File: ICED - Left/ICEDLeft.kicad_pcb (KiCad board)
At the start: 2 copper layers, 175.4 x 145 mm, 164 parts, among them P1 FLASH_HDR, P2 USBC, P3 CONN_17, P4 USB3_AFEMALE, Q1 TC1264, U1 MK20DX256VLH7, U2 IS31FL3731C, X1 CRYSTAL

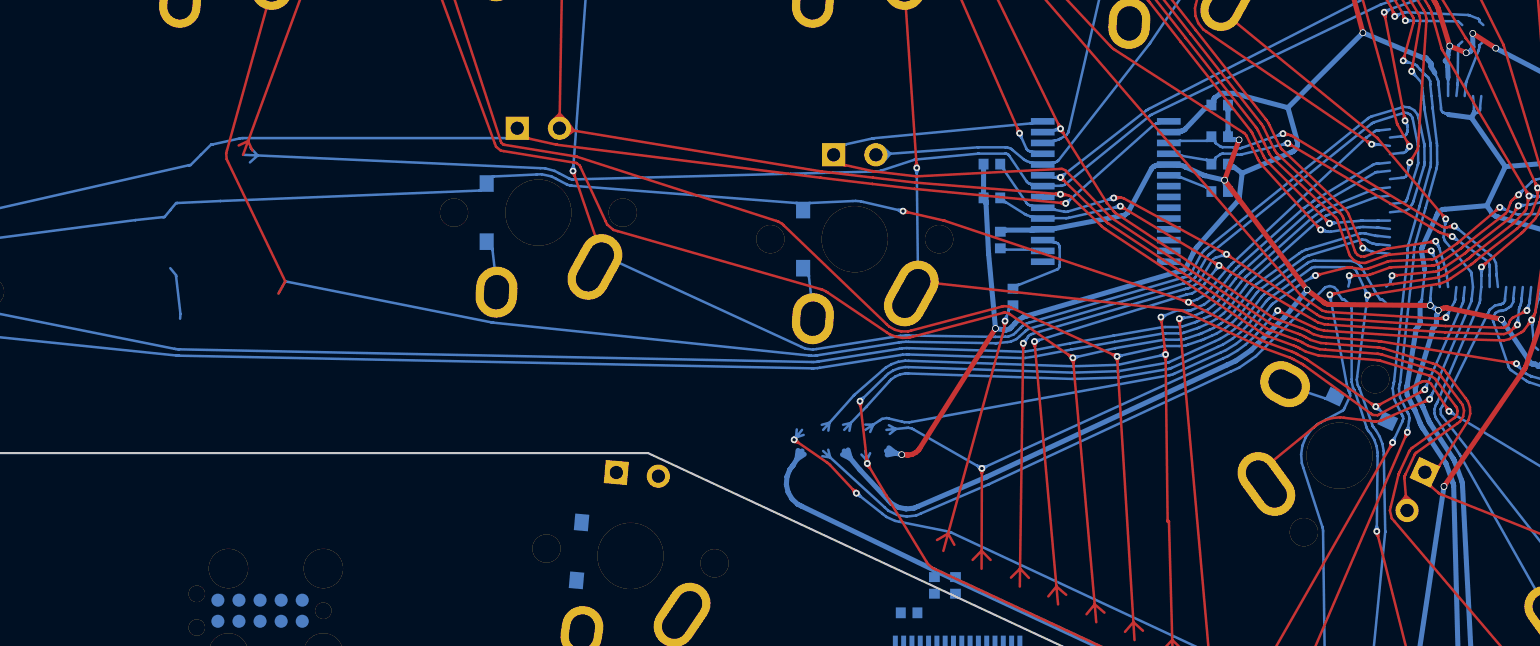
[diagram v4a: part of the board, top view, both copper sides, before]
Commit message: moved U2 and S33-S35
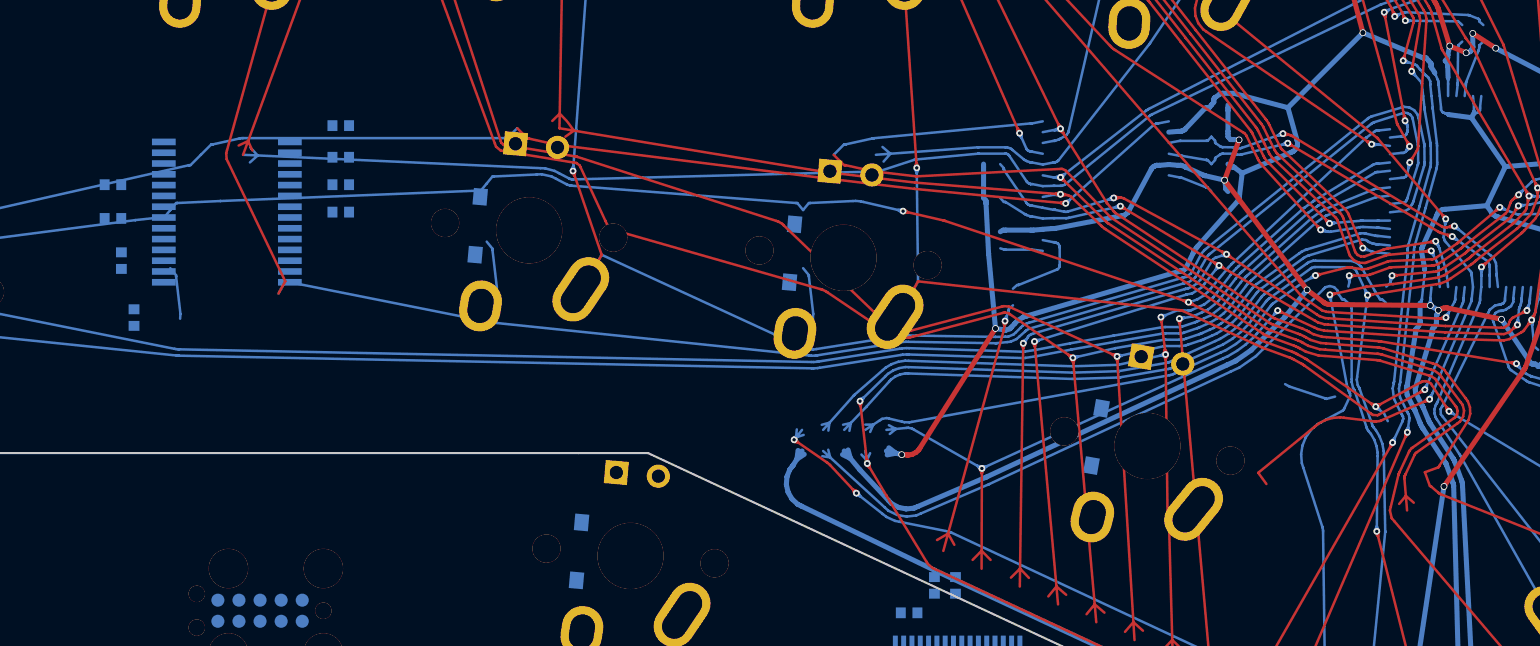
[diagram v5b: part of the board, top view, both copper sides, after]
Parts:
- moved U2 52.9 mm to (69.0, 121.0)
- moved C8 52.9 mm to (63.4, 127.3)
- moved C9 52.9 mm to (62.6, 123.9)
- moved R4 52.9 mm to (62.1, 119.3)
- moved R5 52.9 mm to (62.1, 121.4)
- moved C6 52.9 mm to (75.9, 115.8)
- moved R12 52.9 mm to (75.9, 121.0)
- moved R3 52.9 mm to (75.9, 119.3)
- moved R8 52.9 mm to (75.9, 117.7)
- moved D71 17.2 mm to (125.3, 129.9), turned to 350 degrees
- moved D33 16.0 mm to (121.4, 134.5), turned to 170 degrees
- moved S33 11.6 mm to (124.4, 135.1), turned to 170 degrees
- moved S34 1.31 mm to (106.1, 123.8), turned to 175 degrees
- moved S35 1.20 mm to (87.2, 122.1), turned to 175 degrees
- moved D72 1.13 mm to (106.6, 118.7), turned to 355 degrees
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
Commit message: Checkpoint, moving S32.
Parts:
- moved D70 37.5 mm to (142.5, 111.6), turned to 280 degrees
- moved D32 24.3 mm to (147.0, 117.9), turned to 100 degrees
- moved S32 23.5 mm to (147.5, 120.9), turned to 100 degrees
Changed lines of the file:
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@@
   )
   (module prettylib:INSW_LEDS_REG (layer Front)
-    (at 157.861 145.864 245)
-    (attr smd)
-    (fp_text reference D70 (at 0 -1.5 245) (layer B.SilkS)
-      (effects (font (size 1 1) (thickness 0.2)) (justify mirror))
-    )
-    (fp_text value LED (at 0 2.413 245) (layer F.SilkS) hide
-      (effects (font (thickness 0.3048)))
-    )
-    (pad 2 thru_hole oval (at 1.27 0 245) (size 1.4 1.4) (drill 0.8) (layers *.Cu *.Mask F.SilkS)
+    (at 142.50469 111.64536 280)
+    (attr smd)
+    (fp_text reference D70 (at 0 -1.5 280) (layer B.SilkS)
+      (effects (font (size 1 1) (thickness 0.2)) (justify mirror))
+    )
+    (fp_text value LED (at 0 2.413 280) (layer F.SilkS) hide
+      (effects (font (thickness 0.3048)))
+    )
+    (pad 2 thru_hole oval (at 1.27 0 280) (size 1.4 1.4) (drill 0.8) (layers *.Cu *.Mask F.SilkS)
       (net 3 /ledmatrix/CA2))
-    (pad 1 thru_hole rect (at -1.27 0 245) (size 1.4 1.4) (drill 0.8) (layers *.Cu *.Mask F.SilkS)
+    (pad 1 thru_hole rect (at -1.27 0 280) (size 1.4 1.4) (drill 0.8) (layers *.Cu *.Mask F.SilkS)
       (net 9 /ledmatrix/CA8))
   )
@@
   )
   (module prettylib:SOT123-DIODE (layer Back)
-    (at 154.574 140.899 65)
-    (descr DIODE)
-    (tags DIODE)
-    (attr smd)
-    (fp_text reference D32 (at 0 3.81 335) (layer B.SilkS)
-      (effects (font (size 1.016 1.016) (thickness 0.2032)) (justify mirror))
-    )
-    (fp_text value DIODE (at 2.031999 0 335) (layer B.SilkS) hide
-      (effects (font (thickness 0.3048)) (justify mirror))
-    )
-    (fp_line (start -0.8509 0.70104) (end 0.8509 0.70104) (layer B.SilkS) (width 0.22098))
-    (fp_line (start -0.8509 1.45034) (end -0.59944 1.45034) (layer B.SilkS) (width 0.22098))
-    (fp_line (start 0.8509 1.45034) (end 0.59944 1.45034) (layer B.SilkS) (width 0.22098))
-    (fp_line (start 0.8509 -1.45034) (end 0.59944 -1.45034) (layer B.SilkS) (width 0.22098))
-    (fp_line (start -0.8509 -1.45034) (end -0.59944 -1.45034) (layer B.SilkS) (width 0.22098))
-    (fp_line (start -0.8509 -1.45034) (end -0.8509 1.45034) (layer B.SilkS) (width 0.22098))
-    (fp_line (start 0.8509 -1.45034) (end 0.8509 1.45034) (layer B.SilkS) (width 0.22098))
-    (pad 2 smd rect (at 0 1.7526 155) (size 1.00076 0.8509) (layers Back B.Paste B.Mask)
+    (at 146.96729 117.85944 100)
+    (descr DIODE)
+    (tags DIODE)
+    (attr smd)
+    (fp_text reference D32 (at 0 3.81 370) (layer B.SilkS)
+      (effects (font (size 1.016 1.016) (thickness 0.2032)) (justify mirror))
+    )
+    (fp_text value DIODE (at 2.031999 0 370) (layer B.SilkS) hide
+      (effects (font (thickness 0.3048)) (justify mirror))
+    )
+    (fp_line (start -0.8509 0.70104) (end 0.8509 0.70104) (layer B.SilkS) (width 0.22098))
+    (fp_line (start -0.8509 1.45034) (end -0.59944 1.45034) (layer B.SilkS) (width 0.22098))
+    (fp_line (start 0.8509 1.45034) (end 0.59944 1.45034) (layer B.SilkS) (width 0.22098))
+    (fp_line (start 0.8509 -1.45034) (end 0.59944 -1.45034) (layer B.SilkS) (width 0.22098))
+    (fp_line (start -0.8509 -1.45034) (end -0.59944 -1.45034) (layer B.SilkS) (width 0.22098))
+    (fp_line (start -0.8509 -1.45034) (end -0.8509 1.45034) (layer B.SilkS) (width 0.22098))
+    (fp_line (start 0.8509 -1.45034) (end 0.8509 1.45034) (layer B.SilkS) (width 0.22098))
+    (pad 2 smd rect (at 0 1.7526 190) (size 1.00076 0.8509) (layers Back B.Paste B.Mask)
       (net 101 /Row5))
-    (pad 1 smd rect (at 0 -1.74752 155) (size 1.00076 0.8509) (layers Back B.Paste B.Mask)
+    (pad 1 smd rect (at 0 -1.74752 190) (size 1.00076 0.8509) (layers Back B.Paste B.Mask)
       (net 80 "Net-(D32-Pad1)"))
   )
@@
   )
   (module prettylib:MXALPS (layer Front)
-    (at 153.258 143.718 65)
+    (at 147.50752 120.92323 100)
     (descr MXALPS)
     (tags MXALPS)
-    (fp_text reference S32 (at 0 3.048 65) (layer B.SilkS)
-      (effects (font (thickness 0.3048)) (justify mirror))
-    )
-    (fp_text value SW (at -3.5 9 65) (layer B.SilkS) hide
+    (fp_text reference S32 (at 0 3.048 100) (layer B.SilkS)
+      (effects (font (thickness 0.3048)) (justify mirror))
+    )
+    (fp_text value SW (at -3.5 9 100) (layer B.SilkS) hide
       (effects (font (thickness 0.3048)) (justify mirror))
     )
@@
     (fp_line (start 7.62 7.62) (end -7.62 7.62) (layer Dwgs.User) (width 0.3))
     (fp_line (start -7.62 7.62) (end -7.62 -7.62) (layer Dwgs.User) (width 0.3))
-    (pad "" np_thru_hole circle (at 0 0 65) (size 3.98781 3.98781) (drill 3.9878) (layers *.Cu *.Mask F.SilkS)
+    (pad "" np_thru_hole circle (at 0 0 100) (size 3.98781 3.98781) (drill 3.9878) (layers *.Cu *.Mask F.SilkS)
       (clearance 0.1524))
-    (pad "" np_thru_hole circle (at -5.08 0 65) (size 1.70181 1.70181) (drill 1.7018) (layers *.Cu *.Mask F.SilkS)
+    (pad "" np_thru_hole circle (at -5.08 0 100) (size 1.70181 1.70181) (drill 1.7018) (layers *.Cu *.Mask F.SilkS)
       (clearance 0.1524))
-    (pad "" np_thru_hole circle (at 5.08 0 65) (size 1.70181 1.70181) (drill 1.7018) (layers *.Cu *.Mask F.SilkS)
+    (pad "" np_thru_hole circle (at 5.08 0 100) (size 1.70181 1.70181) (drill 1.7018) (layers *.Cu *.Mask F.SilkS)
       (clearance 0.1524))
-    (pad 1 thru_hole oval (at -3.405 -3.27 35.95) (size 2.5 4.17) (drill oval 1.5 3.17) (layers *.Cu *.Mask F.SilkS)
+    (pad 1 thru_hole oval (at -3.405 -3.27 70.95) (size 2.5 4.17) (drill oval 1.5 3.17) (layers *.Cu *.Mask F.SilkS)
       (net 113 /Col3))
-    (pad 2 thru_hole oval (at 2.52 -4.79 61.1) (size 2.5 3.08) (drill oval 1.5 2.08) (layers *.Cu *.Mask F.SilkS)
+    (pad 2 thru_hole oval (at 2.52 -4.79 96.1) (size 2.5 3.08) (drill oval 1.5 2.08) (layers *.Cu *.Mask F.SilkS)
       (net 80 "Net-(D32-Pad1)"))
   )

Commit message: moved S32
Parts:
- moved D70 13.1 mm to (152.5, 120.0)
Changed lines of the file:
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@@
   )
   (module prettylib:INSW_LEDS_REG (layer Front)
-    (at 142.50469 111.64536 280)
+    (at 152.51034 120.0411 280)
     (attr smd)
     (fp_text reference D70 (at 0 -1.5 280) (layer B.SilkS)

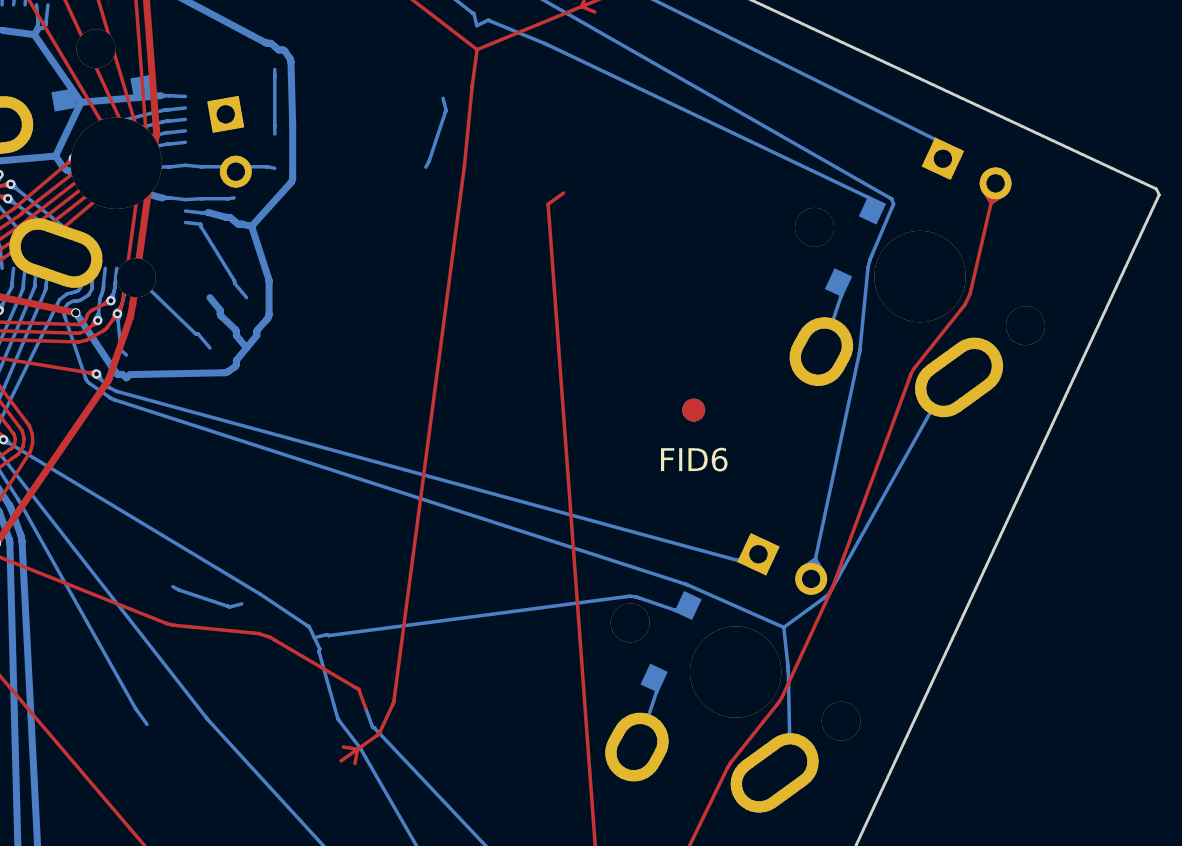
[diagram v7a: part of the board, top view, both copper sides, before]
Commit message: moved S21
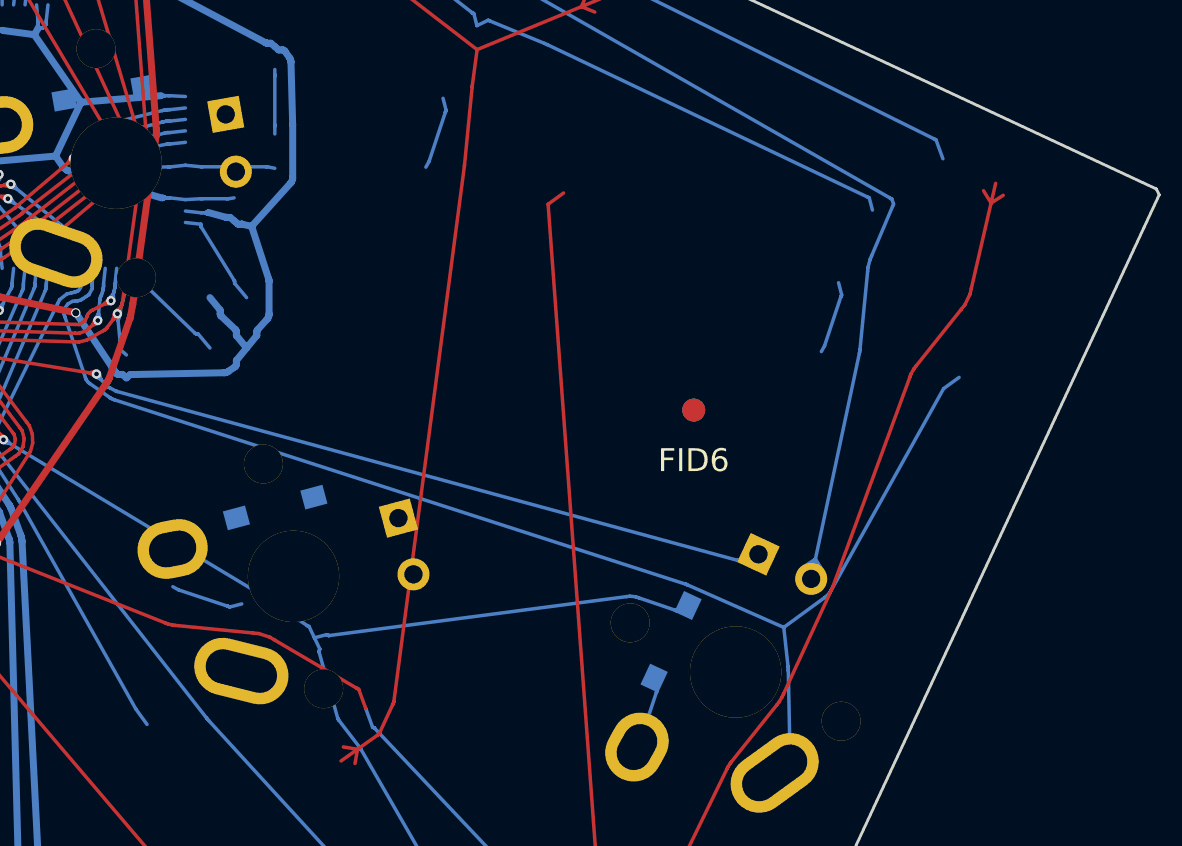
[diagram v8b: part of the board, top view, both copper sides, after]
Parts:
- moved S21 30.3 mm to (155.2, 139.0), turned to 105 degrees
- moved D59 29.5 mm to (160.2, 137.6), turned to 285 degrees
- moved D21 27.8 mm to (154.4, 136.0), turned to 105 degrees
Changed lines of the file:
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@@
   )
   (module prettylib:INSW_LEDS_REG (layer Front)
-    (at 184.747 121.265 335)
-    (attr smd)
-    (fp_text reference D59 (at 0 -1.5 335) (layer B.SilkS)
+    (at 160.15609 137.64268 285)
+    (attr smd)
+    (fp_text reference D59 (at 0 -1.5 285) (layer B.SilkS)
       (effects (font (size 1 1) (thickness 0.2)) (justify mirror))
     )
-    (fp_text value LED (at 0 2.413 335) (layer F.SilkS) hide
+    (fp_text value LED (at 0 2.413 285) (layer F.SilkS) hide
       (effects (font (thickness 0.3048)))
     )
-    (pad 2 thru_hole oval (at 1.27 0 335) (size 1.4 1.4) (drill 0.8) (layers *.Cu *.Mask F.SilkS)
+    (pad 2 thru_hole oval (at 1.27 0 285) (size 1.4 1.4) (drill 0.8) (layers *.Cu *.Mask F.SilkS)
       (net 2 /ledmatrix/CA1))
-    (pad 1 thru_hole rect (at -1.27 0 335) (size 1.4 1.4) (drill 0.8) (layers *.Cu *.Mask F.SilkS)
+    (pad 1 thru_hole rect (at -1.27 0 285) (size 1.4 1.4) (drill 0.8) (layers *.Cu *.Mask F.SilkS)
       (net 7 /ledmatrix/CA6))
   )
@@
   )
   (module prettylib:SOT123-DIODE (layer Back)
-    (at 179.779 124.556 155)
-    (descr DIODE)
-    (tags DIODE)
-    (attr smd)
-    (fp_text reference D21 (at 0 3.81 425) (layer B.SilkS)
-      (effects (font (size 1.016 1.016) (thickness 0.2032)) (justify mirror))
-    )
-    (fp_text value DIODE (at 2.031999 0 425) (layer B.SilkS) hide
-      (effects (font (thickness 0.3048)) (justify mirror))
-    )
-    (fp_line (start -0.8509 0.70104) (end 0.8509 0.70104) (layer B.SilkS) (width 0.22098))
-    (fp_line (start -0.8509 1.45034) (end -0.59944 1.45034) (layer B.SilkS) (width 0.22098))
-    (fp_line (start 0.8509 1.45034) (end 0.59944 1.45034) (layer B.SilkS) (width 0.22098))
-    (fp_line (start 0.8509 -1.45034) (end 0.59944 -1.45034) (layer B.SilkS) (width 0.22098))
-    (fp_line (start -0.8509 -1.45034) (end -0.59944 -1.45034) (layer B.SilkS) (width 0.22098))
-    (fp_line (start -0.8509 -1.45034) (end -0.8509 1.45034) (layer B.SilkS) (width 0.22098))
-    (fp_line (start 0.8509 -1.45034) (end 0.8509 1.45034) (layer B.SilkS) (width 0.22098))
-    (pad 2 smd rect (at 0 1.7526 245) (size 1.00076 0.8509) (layers Back B.Paste B.Mask)
+    (at 154.44421 135.95325 105)
+    (descr DIODE)
+    (tags DIODE)
+    (attr smd)
+    (fp_text reference D21 (at 0 3.81 325) (layer B.SilkS)
+      (effects (font (size 1.016 1.016) (thickness 0.2032)) (justify mirror))
+    )
+    (fp_text value DIODE (at 2.031999 0 325) (layer B.SilkS) hide
+      (effects (font (thickness 0.3048)) (justify mirror))
+    )
+    (fp_line (start -0.8509 0.70104) (end 0.8509 0.70104) (layer B.SilkS) (width 0.22098))
+    (fp_line (start -0.8509 1.45034) (end -0.59944 1.45034) (layer B.SilkS) (width 0.22098))
+    (fp_line (start 0.8509 1.45034) (end 0.59944 1.45034) (layer B.SilkS) (width 0.22098))
+    (fp_line (start 0.8509 -1.45034) (end 0.59944 -1.45034) (layer B.SilkS) (width 0.22098))
+    (fp_line (start -0.8509 -1.45034) (end -0.59944 -1.45034) (layer B.SilkS) (width 0.22098))
+    (fp_line (start -0.8509 -1.45034) (end -0.8509 1.45034) (layer B.SilkS) (width 0.22098))
+    (fp_line (start 0.8509 -1.45034) (end 0.8509 1.45034) (layer B.SilkS) (width 0.22098))
+    (pad 2 smd rect (at 0 1.7526 195) (size 1.00076 0.8509) (layers Back B.Paste B.Mask)
       (net 100 /Row4))
-    (pad 1 smd rect (at 0 -1.74752 245) (size 1.00076 0.8509) (layers Back B.Paste B.Mask)
+    (pad 1 smd rect (at 0 -1.74752 195) (size 1.00076 0.8509) (layers Back B.Paste B.Mask)
       (net 69 "Net-(D21-Pad1)"))
   )
@@
   )
   (module prettylib:MXALPS (layer Front)
-    (at 182.598 125.87 155)
-    (descr MXALPS)
-    (tags MXALPS)
-    (fp_text reference S21 (at 0 3.048 155) (layer B.SilkS)
-      (effects (font (thickness 0.3048)) (justify mirror))
-    )
-    (fp_text value SW (at -3.5 9 155) (layer B.SilkS) hide
-      (effects (font (thickness 0.3048)) (justify mirror))
-    )
-    (fp_line (start -7.75 6.4) (end -7.75 -6.4) (layer Dwgs.User) (width 0.3))
-    (fp_line (start -7.75 6.4) (end 7.75 6.4) (layer Dwgs.User) (width 0.3))
-    (fp_line (start 7.75 6.4) (end 7.75 -6.4) (layer Dwgs.User) (width 0.3))
-    (fp_line (start 7.75 -6.4) (end -7.75 -6.4) (layer Dwgs.User) (width 0.3))
-    (fp_line (start -7.62 -7.62) (end 7.62 -7.62) (layer Dwgs.User) (width 0.3))
-    (fp_line (start 7.62 -7.62) (end 7.62 7.62) (layer Dwgs.User) (width 0.3))
-    (fp_line (start 7.62 7.62) (end -7.62 7.62) (layer Dwgs.User) (width 0.3))
-    (fp_line (start -7.62 7.62) (end -7.62 -7.62) (layer Dwgs.User) (width 0.3))
-    (pad "" np_thru_hole circle (at 0 0 155) (size 3.98781 3.98781) (drill 3.9878) (layers *.Cu *.Mask F.SilkS)
-      (clearance 0.1524))
-    (pad "" np_thru_hole circle (at -5.08 0 155) (size 1.70181 1.70181) (drill 1.7018) (layers *.Cu *.Mask F.SilkS)
-      (clearance 0.1524))
-    (pad "" np_thru_hole circle (at 5.08 0 155) (size 1.70181 1.70181) (drill 1.7018) (layers *.Cu *.Mask F.SilkS)
-      (clearance 0.1524))
-    (pad 1 thru_hole oval (at -3.405 -3.27 125.95) (size 2.5 4.17) (drill oval 1.5 3.17) (layers *.Cu *.Mask F.SilkS)
+    (at 155.24919 138.95748 105)
+    (descr MXALPS)
+    (tags MXALPS)
+    (fp_text reference S21 (at 0 3.048 105) (layer B.SilkS)
+      (effects (font (thickness 0.3048)) (justify mirror))
+    )
+    (fp_text value SW (at -3.5 9 105) (layer B.SilkS) hide
+      (effects (font (thickness 0.3048)) (justify mirror))
+    )
+    (fp_line (start -7.75 6.4) (end -7.75 -6.4) (layer Dwgs.User) (width 0.3))
+    (fp_line (start -7.75 6.4) (end 7.75 6.4) (layer Dwgs.User) (width 0.3))
+    (fp_line (start 7.75 6.4) (end 7.75 -6.4) (layer Dwgs.User) (width 0.3))
+    (fp_line (start 7.75 -6.4) (end -7.75 -6.4) (layer Dwgs.User) (width 0.3))
+    (fp_line (start -7.62 -7.62) (end 7.62 -7.62) (layer Dwgs.User) (width 0.3))
+    (fp_line (start 7.62 -7.62) (end 7.62 7.62) (layer Dwgs.User) (width 0.3))
+    (fp_line (start 7.62 7.62) (end -7.62 7.62) (layer Dwgs.User) (width 0.3))
+    (fp_line (start -7.62 7.62) (end -7.62 -7.62) (layer Dwgs.User) (width 0.3))
+    (pad "" np_thru_hole circle (at 0 0 105) (size 3.98781 3.98781) (drill 3.9878) (layers *.Cu *.Mask F.SilkS)
+      (clearance 0.1524))
+    (pad "" np_thru_hole circle (at -5.08 0 105) (size 1.70181 1.70181) (drill 1.7018) (layers *.Cu *.Mask F.SilkS)
+      (clearance 0.1524))
+    (pad "" np_thru_hole circle (at 5.08 0 105) (size 1.70181 1.70181) (drill 1.7018) (layers *.Cu *.Mask F.SilkS)
+      (clearance 0.1524))
+    (pad 1 thru_hole oval (at -3.405 -3.27 75.95) (size 2.5 4.17) (drill oval 1.5 3.17) (layers *.Cu *.Mask F.SilkS)
       (net 120 /Col1))
-    (pad 2 thru_hole oval (at 2.52 -4.79 151.1) (size 2.5 3.08) (drill oval 1.5 2.08) (layers *.Cu *.Mask F.SilkS)
+    (pad 2 thru_hole oval (at 2.52 -4.79 101.1) (size 2.5 3.08) (drill oval 1.5 2.08) (layers *.Cu *.Mask F.SilkS)
       (net 69 "Net-(D21-Pad1)"))
   )
